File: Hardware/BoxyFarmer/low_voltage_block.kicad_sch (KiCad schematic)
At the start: 24 parts

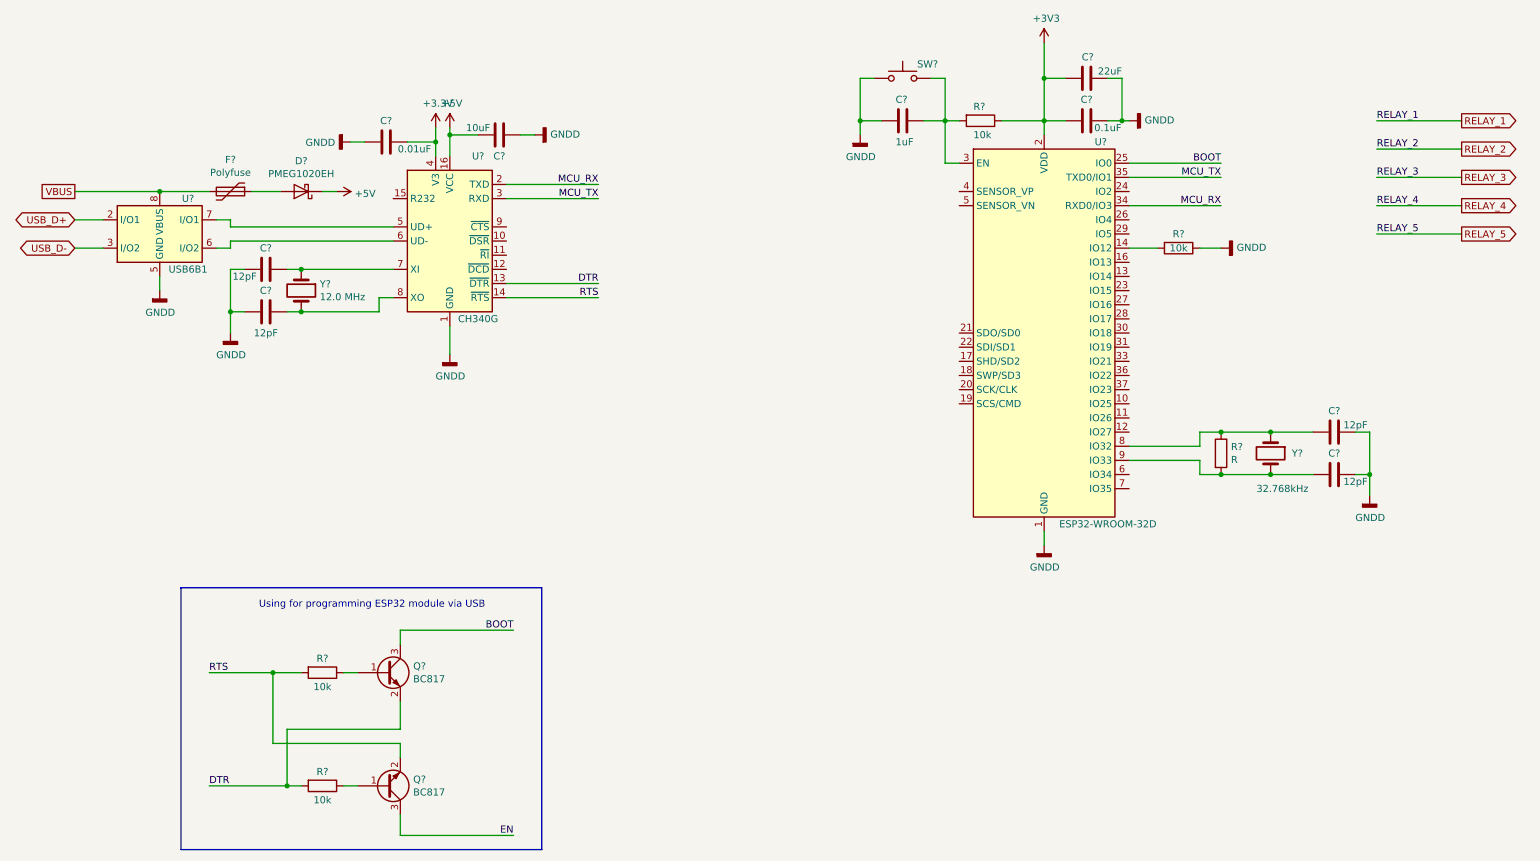
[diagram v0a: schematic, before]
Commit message: Changed Schematic structure, USB connector type changed from MicroUSB to MiniUSB
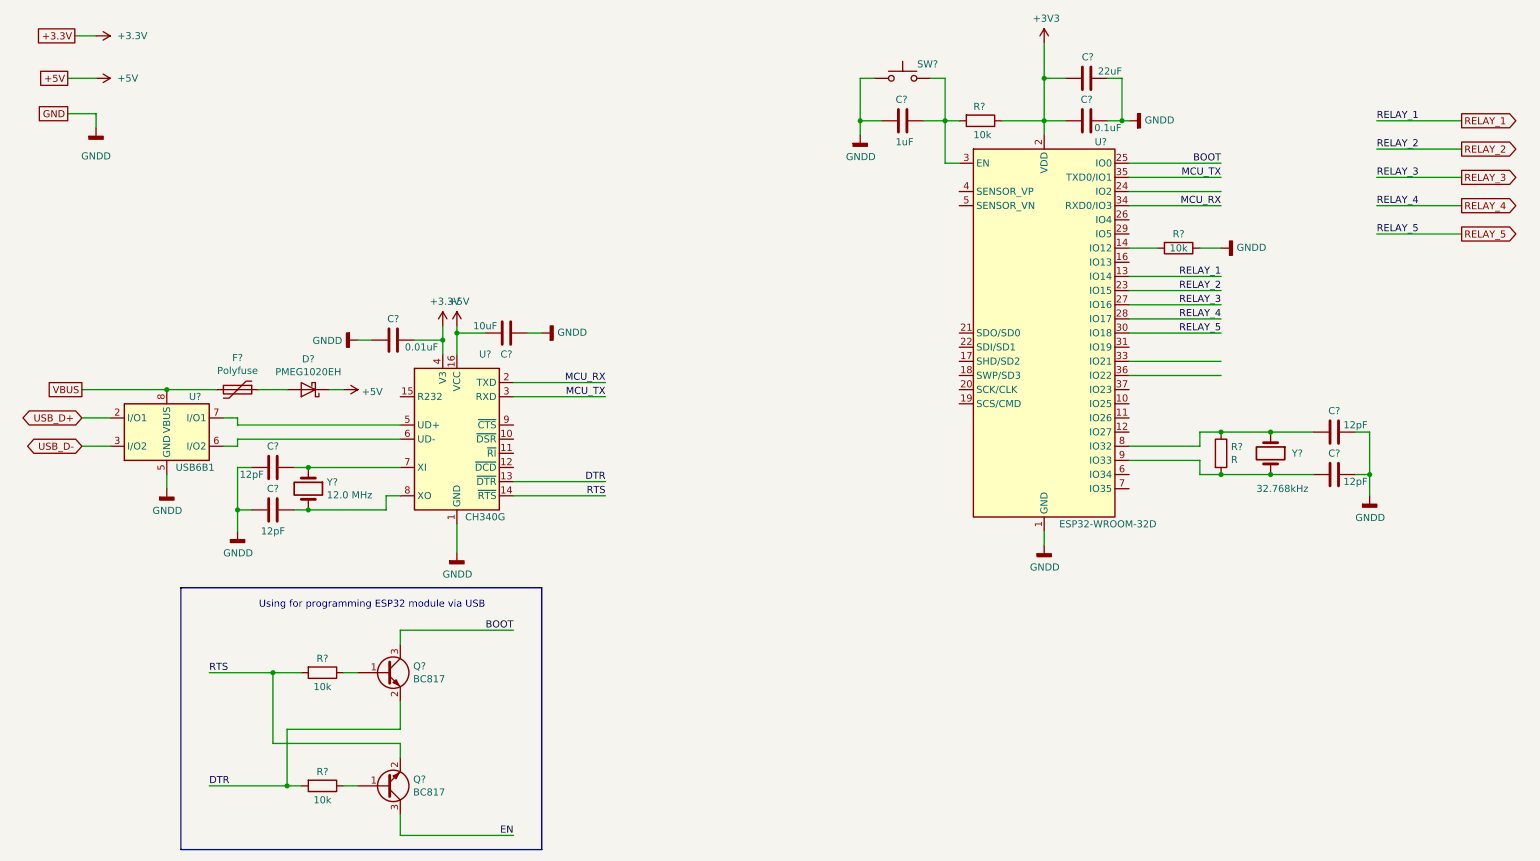
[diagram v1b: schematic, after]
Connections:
- net RELAY_1: now also U?.13 (IO14)
- net RELAY_2: now also U?.23 (IO15)
- net RELAY_3: now also U?.27 (IO16)
- net RELAY_4: now also U?.28 (IO17)
- net RELAY_5: now also U?.30 (IO18)
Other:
- title: (none) -> BoxyFarmer
- moved on the sheet: C?, D?, F?, U?, Y?
